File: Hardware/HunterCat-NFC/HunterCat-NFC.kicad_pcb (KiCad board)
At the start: 2 copper layers, 80.7 x 33.5 mm, 71 parts, among them J1 Battery, J2 Conn_01x06_Female, P1 USB_C_Plug_USB2.0, Q1 DMG3415U-7, SW1 RESET, SW2 GPIO, SW3 GPIO1, SW4 GPIO2, SW5 ON, U1 ATSAMD21E18A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

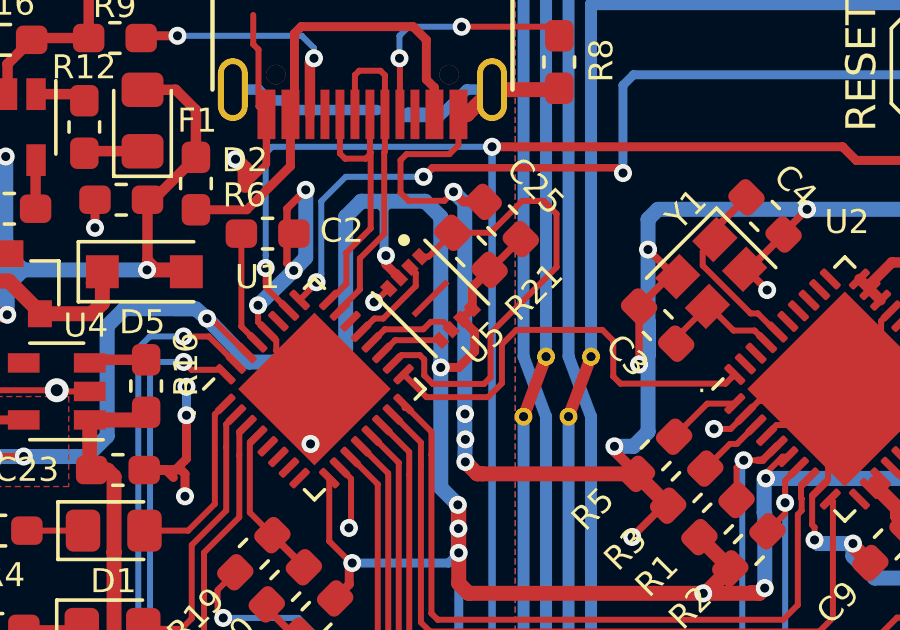
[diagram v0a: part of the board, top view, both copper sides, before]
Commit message: update flash memmory
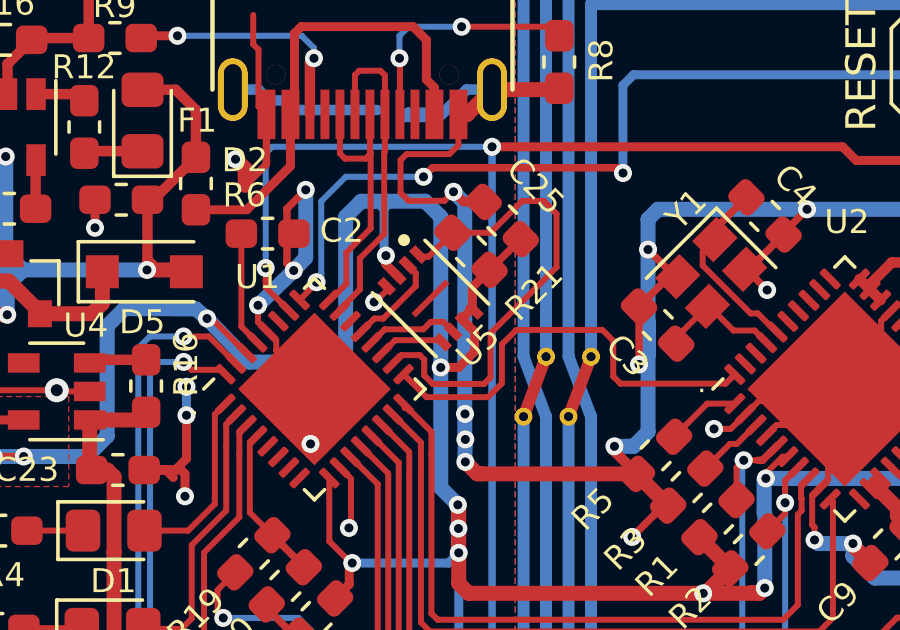
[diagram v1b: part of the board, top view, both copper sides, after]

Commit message: update case
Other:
- rule pad_to_mask_clearance: 0.051 -> 0
- board text added: "V1.3"
- board text removed: "V1.2"
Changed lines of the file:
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@@
   (title_block
     (title "Hunter Cat NFC")
-    (date 2020-11-30)
-    (rev v1.2)
+    (date 2021-01-20)
+    (rev v1.3)
     (company "Electronic Cats")
     (comment 1 "Eduardo Contreras")
@@
     (pad_size 0.65 0.65)
     (pad_drill 0.65)
-    (pad_to_mask_clearance 0.051)
-    (solder_mask_min_width 0.25)
+    (pad_to_mask_clearance 0)
     (aux_axis_origin 0 0)
     (visible_elements 7FFFFFFF)
@@
       (drillshape 0)
       (scaleselection 1)
-      (outputdirectory "gerbers_hunterNFC_v1.2/"))
+      (outputdirectory "gerbers_hunterNFC_v1.3/"))
   )
   (net 0 "")
@@
       (effects (font (size 0.5 0.5) (thickness 0.08)))
     )
-    (pad 2 smd roundrect (at 1.025 0) (size 1.15 1.4) (layers F.Cu F.Paste F.Mask) (roundrect_rratio 0.217391)
+    (pad 2 smd roundrect (at 1.025 0) (size 1.15 1.4) (layers F.Cu F.Paste F.Mask) (roundrect_rratio 0.2173904347826087)
       (net 17 /LED1))
-    (pad 1 smd roundrect (at -1.025 0) (size 1.15 1.4) (layers F.Cu F.Paste F.Mask) (roundrect_rratio 0.217391)
+    (pad 1 smd roundrect (at -1.025 0) (size 1.15 1.4) (layers F.Cu F.Paste F.Mask) (roundrect_rratio 0.2173904347826087)
       (net 18 "Net-(D1-Pad1)"))
     (model ${KISYS3DMOD}/LED_SMD.3dshapes/LED_0805_2012Metric.wrl
@@
       (effects (font (size 0.5 0.5) (thickness 0.08)))
     )
-    (pad 2 smd roundrect (at 1.025 0 90) (size 1.15 1.4) (layers F.Cu F.Paste F.Mask) (roundrect_rratio 0.217391)
+    (pad 2 smd roundrect (at 1.025 0 90) (size 1.15 1.4) (layers F.Cu F.Paste F.Mask) (roundrect_rratio 0.2173904347826087)
       (net 16 VBUS))
-    (pad 1 smd roundrect (at -1.025 0 90) (size 1.15 1.4) (layers F.Cu F.Paste F.Mask) (roundrect_rratio 0.217391)
+    (pad 1 smd roundrect (at -1.025 0 90) (size 1.15 1.4) (layers F.Cu F.Paste F.Mask) (roundrect_rratio 0.2173904347826087)
       (net 19 "Net-(D2-Pad1)"))
     (model ${KISYS3DMOD}/LED_SMD.3dshapes/LED_0805_2012Metric.wrl
@@
       (effects (font (size 0.5 0.5) (thickness 0.08)))
     )
-    (pad 1 smd roundrect (at -1.025 0) (size 1.15 1.4) (layers F.Cu F.Paste F.Mask) (roundrect_rratio 0.217391)
+    (pad 1 smd roundrect (at -1.025 0) (size 1.15 1.4) (layers F.Cu F.Paste F.Mask) (roundrect_rratio 0.2173904347826087)
       (net 21 "Net-(D3-Pad1)"))
-    (pad 2 smd roundrect (at 1.025 0) (size 1.15 1.4) (layers F.Cu F.Paste F.Mask) (roundrect_rratio 0.217391)
+    (pad 2 smd roundrect (at 1.025 0) (size 1.15 1.4) (layers F.Cu F.Paste F.Mask) (roundrect_rratio 0.2173904347826087)
       (net 20 /LED2))
     (model ${KISYS3DMOD}/LED_SMD.3dshapes/LED_0805_2012Metric.wrl
@@
       (effects (font (size 0.5 0.5) (thickness 0.08)))
     )
-    (pad 1 smd roundrect (at -1.025 0) (size 1.15 1.4) (layers F.Cu F.Paste F.Mask) (roundrect_rratio 0.217391)
+    (pad 1 smd roundrect (at -1.025 0) (size 1.15 1.4) (layers F.Cu F.Paste F.Mask) (roundrect_rratio 0.2173904347826087)
       (net 23 "Net-(D4-Pad1)"))
-    (pad 2 smd roundrect (at 1.025 0) (size 1.15 1.4) (layers F.Cu F.Paste F.Mask) (roundrect_rratio 0.217391)
+    (pad 2 smd roundrect (at 1.025 0) (size 1.15 1.4) (layers F.Cu F.Paste F.Mask) (roundrect_rratio 0.2173904347826087)
       (net 22 /LED3))
     (model ${KISYS3DMOD}/LED_SMD.3dshapes/LED_0805_2012Metric.wrl
@@
   (gr_line (start 157.69 108.99) (end 83 109) (layer Edge.Cuts) (width 0.05))
   (gr_line (start 160.69 78.5) (end 160.69 105.99) (layer Edge.Cuts) (width 0.05))
-  (gr_text V1.2 (at 104.91 92.61 90) (layer B.SilkS)
+  (gr_text V1.3 (at 104.91 92.61 90) (layer B.SilkS)
     (effects (font (size 1 1) (thickness 0.2)) (justify mirror))
   )

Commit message: Change_Crystal
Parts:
- Y1: footprint Crystal:Crystal_SMD_2520-4Pin_2.5x2.0mm -> Crystal:Crystal_SMD_2016-4Pin_2.0x1.6mm
- moved C3 0.60 mm to (128.1, 89.7)
- moved Y1 0.46 mm to (129.8, 88.2), turned to 45 degrees
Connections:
- J2 pad 6: Net-(J2-Pad6) -> unconnected-(J2-Pad6)
- U1 pad 22: Net-(U1-Pad22) -> unconnected-(U1-Pad22)
- U1 pad 27: Net-(U1-Pad27) -> unconnected-(U1-Pad27)
- U1 pad 5: Net-(U1-Pad5) -> unconnected-(U1-Pad5)
- U1 pad 6: Net-(U1-Pad6) -> unconnected-(U1-Pad6)
- U1 pad 7: Net-(U1-Pad7) -> unconnected-(U1-Pad7)
- U1 pad 8: Net-(U1-Pad8) -> unconnected-(U1-Pad8)
- U4 pad 4: Net-(U4-Pad4) -> unconnected-(U4-Pad4)
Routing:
- net Net-(C4-Pad1): track 6.28 -> 12.0 mm
- net Net-(C3-Pad1): track 4.15 -> 9.19 mm
- net GND: track 284.8 -> 282.8 mm, vias 43 -> 42
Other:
- net class Default removed

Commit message: update labels for v1.4
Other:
- board text added: "V1.4"
- board text removed: "&"
- board text removed: "Salvador Mendoza"
- board text removed: "V1.3"
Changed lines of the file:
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@@
     (43 "Eco2.User" user "User.Eco2")
     (44 "Edge.Cuts" user)
-    (45 "Margin" user)
+    (45 "Margin" user "Margen")
     (46 "B.CrtYd" user "B.Courtyard")
     (47 "F.CrtYd" user "F.Courtyard")
@@
     (effects (font (size 1.2 1.2) (thickness 0.3)) (justify mirror))
   )
-  (gr_text "Salvador Mendoza" (at 99.61 92.61 90) (layer "B.SilkS")
-    (effects (font (size 1 1) (thickness 0.25)) (justify mirror))
-  )
-  (gr_text "V1.3" (at 104.91 92.61 90) (layer "B.SilkS")
+  (gr_text "V1.4" (at 104.91 92.61 90) (layer "B.SilkS")
     (effects (font (size 1 1) (thickness 0.2)) (justify mirror))
   )
@@
     (effects (font (size 2 2) (thickness 0.5)) (justify mirror))
   )
-  (gr_text "&" (at 96.69 92.37 90) (layer "B.SilkS")
-    (effects (font (size 1 1) (thickness 0.25)) (justify mirror))
-  )
   (gr_text "." (at 129.1 92.03) (layer "F.SilkS")

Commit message: Starting the change of PCB design
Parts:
- added C15: 27pF, Capacitor_SMD:C_0603_1608Metric, F.Cu at (145.4, 72.4)
- added C17: 0.1uF, Capacitor_SMD:C_0603_1608Metric, F.Cu at (155.7, 68.1)
- added C21: 0.1uF, Capacitor_SMD:C_0603_1608Metric, F.Cu at (153.8, 58.1)
- added C22: 1uF, Capacitor_SMD:C_0603_1608Metric, F.Cu at (155.7, 65.6)
- added C25: 0.1uF, Capacitor_SMD:C_0603_1608Metric, F.Cu at (145.4, 69.9)
- added C26: 0.1uF, Capacitor_SMD:C_0603_1608Metric, F.Cu at (143.7, 67.3)
- added C27: 0.1uF, Capacitor_SMD:C_0603_1608Metric, F.Cu at (157.8, 63.1)
- added C28: 0.1uF, Capacitor_SMD:C_0603_1608Metric, F.Cu at (149.4, 69.9)
- added C29: 0.1uF, Capacitor_SMD:C_0603_1608Metric, F.Cu at (157.8, 58.1)
- added C30: 0.1uF, Capacitor_SMD:C_0603_1608Metric, F.Cu at (141.4, 71.9)
- added C31: 0.1uF, Capacitor_SMD:C_0603_1608Metric, F.Cu at (141.4, 74.5)
- added C32: 0.1uF, Capacitor_SMD:C_0603_1608Metric, F.Cu at (161.8, 58.1)
- added R22: 27, Resistor_SMD:R_0603_1608Metric, F.Cu at (151.7, 67.3)
- added R23: 1K, Resistor_SMD:R_0603_1608Metric, F.Cu at (147.7, 67.3)
- added R24: 10K, Resistor_SMD:R_0603_1608Metric, F.Cu at (149.4, 72.4)
- added R7: 1K, Resistor_SMD:R_0603_1608Metric, F.Cu at (161.8, 60.6)
- added SW6: BOOT, Button_Switch_SMD:SW_SPST_TL3342, F.Cu at (136.9, 67.2)
- added Y2: 12Mhz, Crystal:Crystal_SMD_5032-2Pin_5.0x3.2mm, F.Cu at (135.8, 73.1)
- C1: value 0.1uF -> 27pF; footprint Capacitor_SMD:C_0603_1608Metric_Pad1.05x0.95mm_HandSolder -> Capacitor_SMD:C_0603_1608Metric
- C2: footprint Capacitor_SMD:C_0603_1608Metric_Pad1.05x0.95mm_HandSolder -> Capacitor_SMD:C_0603_1608Metric
- R17, R18, R4: value 1K -> 330
- R21: value 10K -> 27; footprint Resistor_SMD:R_0603_1608Metric_Pad1.05x0.95mm_HandSolder -> Resistor_SMD:R_0603_1608Metric
- U1: value ATSAMD21E18A -> RP2040; footprint Package_DFN_QFN:QFN-32-1EP_5x5mm_P0.5mm_EP3.6x3.6mm -> RP2040:RP2040-QFN-56
- U5: value GD25Q16CEIGR -> W25Q16JV; footprint hunter-cat-nfc:PSON50P200X300X50-9N -> Package_SO:SOIC-8_5.275x5.275mm_P1.27mm
- moved C1 52.5 mm to (153.8, 63.1), turned to 0 degrees
- moved C2 47.3 mm to (153.8, 60.6)
- moved R21 45.4 mm to (157.8, 60.6), turned to 0 degrees
- moved U5 33.8 mm to (137.3, 60.2), turned to 0 degrees
- moved R19 5.96 mm to (113.4, 103.7), turned to 0 degrees
- moved Re 3.82 mm to (113.4, 102.2), turned to 180 degrees
- moved U1 3.46 mm to (116.5, 95.7), turned to 0 degrees
- moved D4 2.62 mm to (109.5, 100.8)
- moved R18 2.62 mm to (105.6, 100.7)
- moved J2 2.42 mm to (118.5, 106.1)
- moved D3 1.40 mm to (109.5, 98.8)
- moved R17 1.40 mm to (105.6, 98.8)
- moved C25 0.42 mm to (122.8, 86.4)
- renumbered R20 to Re
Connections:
- C1 pad 1: +3V3 -> Net-(C1-Pad1)
- C2 pad 1: Net-(C2-Pad1) -> +1V2
- R21 pad 1: +3V3 -> /D+
- R21 pad 2: /CS -> /RD+
- U1 pad 1: /LED1 -> +3V3
- U1 pad 10: GND -> +3V3
- U1 pad 11: /SDA -> unconnected-(U1-Pad11)
- U1 pad 12: /SCL -> unconnected-(U1-Pad12)
- U1 pad 13: /GPIO2 -> unconnected-(U1-Pad13)
- U1 pad 14: /GPIO1 -> unconnected-(U1-Pad14)
- U1 pad 15: /VEN -> unconnected-(U1-Pad15)
- U1 pad 16: /IRQ -> unconnected-(U1-Pad16)
- U1 pad 17: /CLK -> /VEN
- U1 pad 18: /CS -> /IRQ
- U1 pad 19: /MOSI -> GND
- U1 pad 2: /LED2 -> /TX
- U1 pad 20: /SCK -> Net-(C1-Pad1)
- U1 pad 21: /MISO -> Net-(R7-Pad2)
- U1 pad 22: unconnected-(U1-Pad22) -> +3V3
- U1 pad 23: /D- -> +1V2
- U1 pad 24: /D+ -> /SWCLK
- U1 pad 25: /GPIO -> /SWDIO
- U1 pad 27: unconnected-(U1-Pad27) -> /CLK
- U1 pad 28: GND -> /GPIO
- U1 pad 29: Net-(C2-Pad1) -> unconnected-(U1-Pad29)
- U1 pad 3: /LED3 -> /RX
- U1 pad 30: +3V3 -> unconnected-(U1-Pad30)
- U1 pad 31: /SWCLK -> unconnected-(U1-Pad31)
- U1 pad 32: /SWDIO -> /GPIO1
- U1 pad 4: /B_ADC -> unconnected-(U1-Pad4)
- U1 pad 6: unconnected-(U1-Pad6) -> /SDA
- U1 pad 7: unconnected-(U1-Pad7) -> /SCL
- U1 pad 9: +3V3 -> unconnected-(U1-Pad9)
- U4 pad 3: Net-(R16-Pad2) -> Net-(C23-Pad1)
- U5 pad 1: /CS -> /QSPI_CS
- U5 pad 2: /MISO -> /QSPI_DATA1
- U5 pad 3: +3V3 -> /QSPI_DATA2
- U5 pad 5: /MOSI -> /QSPI_DATA0
- U5 pad 6: /SCK -> /QSPI_SCK
- U5 pad 7: +3V3 -> /QSPI_DATA3
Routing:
- net GND: track 282.8 -> 257.1 mm, vias 42 -> 32
- net +3V3: track 134.0 -> 109.3 mm, vias 17 -> 16
- net /SWCLK: track 25.4 -> 1.84 mm, vias 2 -> 0
- net /VEN: track 25.4 -> 2.20 mm
- net /IRQ: track 24.2 -> 1.84 mm
- net /CS: track 16.6 -> 0.00 mm
- net /RST: track 62.5 -> 49.0 mm, vias 3 -> 2
- net /SWDIO: track 19.8 -> 6.59 mm, vias 2 -> 0
- net +BATT: track 56.1 -> 44.9 mm
- net /LED3: track 12.2 -> 1.44 mm
- net /CLK: track 14.6 -> 3.94 mm
- net /LED2: track 9.17 -> 1.76 mm
- net /SCL: track 29.9 -> 22.7 mm
- net /SDA: track 30.2 -> 23.0 mm
- net /GPIO2: track 43.5 -> 36.3 mm
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
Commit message: update layout to 3.0v
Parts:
- removed the C25 at (122.8, 86.4)
- removed J2: Conn_01x06_Female, Connector:Tag-Connect_TC2030-IDC-NL_2x03_P1.27mm_Vertical
- removed R16: 10K, Resistor_SMD:R_0603_1608Metric_Pad1.05x0.95mm_HandSolder
- removed R23: 1K, Resistor_SMD:R_0603_1608Metric
- removed Re: 100K, Resistor_SMD:R_0603_1608Metric_Pad1.05x0.95mm_HandSolder
- removed SW6: BOOT, Button_Switch_SMD:SW_SPST_TL3342
- added JP1: BOOT, Jumper:SolderJumper-2_P1.3mm_Open_TrianglePad1.0x1.5mm, B.Cu at (113.1, 87.5)
- added R20: 100K, Resistor_SMD:R_0603_1608Metric, F.Cu at (109.1, 76.7)
- C10, C11, C12, C13, C14, C16, C18, C19, C20, C23, C24, C3, C4, C5, C6, C7, C8, C9: footprint Capacitor_SMD:C_0603_1608Metric_Pad1.05x0.95mm_HandSolder -> Capacitor_SMD:C_0603_1608Metric
- R1, R10, R11, R12, R13, R14, R15, R17, R18, R19, R2, R3, R4, R5, R6, R8, R9: footprint Resistor_SMD:R_0603_1608Metric_Pad1.05x0.95mm_HandSolder -> Resistor_SMD:R_0603_1608Metric
- U5: footprint Package_SO:SOIC-8_5.275x5.275mm_P1.27mm -> hunter-cat-nfc:W25Q16JVUUIQ
- Y2: footprint Crystal:Crystal_SMD_5032-2Pin_5.0x3.2mm -> Crystal:Crystal_SMD_2520-4Pin_2.5x2.0mm
- moved R7 61.1 mm to (116.1, 101.1)
- moved C1 58.1 mm to (111.9, 103.3), turned to 90 degrees
- moved C27 54.4 mm to (120.5, 102.6)
- moved C22 54.1 mm to (109.7, 94.0), turned to -90 degrees
- moved C32 53.6 mm to (116.0, 86.0), turned to 90 degrees
- moved C2 52.5 mm to (120.5, 101.2)
- moved C29 49.1 mm to (117.5, 86.0), turned to 90 degrees
- moved R21 48.2 mm to (118.9, 88.9), turned to -90 degrees
- moved C21 44.4 mm to (121.8, 88.9), turned to 90 degrees
- moved C28 44.4 mm to (111.5, 93.0), turned to 90 degrees
- moved C17 44.2 mm to (116.8, 89.0), turned to 90 degrees
- moved C26 43.5 mm to (120.5, 104.1)
- moved C15 42.2 mm to (116.8, 103.3), turned to -90 degrees
- moved C30 39.6 mm to (120.5, 105.6)
- moved R24 38.3 mm to (113.4, 85.5), turned to 180 degrees
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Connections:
- U1 pad 11: unconnected-(U1-Pad11) -> /LED1
- U1 pad 12: unconnected-(U1-Pad12) -> /LED2
- U1 pad 13: unconnected-(U1-Pad13) -> /LED3
- U1 pad 17: /VEN -> unconnected-(U1-Pad17)
- U1 pad 18: /IRQ -> unconnected-(U1-Pad18)
- U1 pad 27: /CLK -> unconnected-(U1-Pad27)
- U1 pad 28: /GPIO -> /VEN
- U1 pad 29: unconnected-(U1-Pad29) -> /IRQ
- U1 pad 30: unconnected-(U1-Pad30) -> /GPIO2
- U1 pad 31: unconnected-(U1-Pad31) -> /GPIO
- U1 pad 34: /GPIO2 -> unconnected-(U1-Pad34)
- U1 pad 37: /LED1 -> unconnected-(U1-Pad37)
- U1 pad 39: /LED2 -> unconnected-(U1-Pad39)
- U1 pad 40: /LED3 -> unconnected-(U1-Pad40)
- U2 pad 40: /CLK -> unconnected-(U2-Pad40)
- Y2 pad 2: Net-(C15-Pad1) -> GND
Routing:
- net +3V3: track 109.3 -> 153.2 mm, vias 16 -> 11
- net /B_ADC: track 1.50 -> 42.0 mm, vias 0 -> 2
- net +BATT: track 44.9 -> 11.5 mm, vias 2 -> 0
- net +1V2: track 0.00 -> 25.3 mm
- net /VEN: track 2.20 -> 19.1 mm
- net /IRQ: track 1.84 -> 18.1 mm
- net /QSPI_CS: track 0.00 -> 13.5 mm, vias 0 -> 1
- net /SCL: track 22.7 -> 35.4 mm, vias 2 -> 4
- net /SDA: track 23.0 -> 35.1 mm, vias 2 -> 4
- net /GPIO: track 43.4 -> 52.8 mm, vias 4 -> 5
- net /QSPI_DATA1: track 0.00 -> 8.32 mm
- net /RST: track 49.0 -> 40.7 mm
- net Net-(C1-Pad1): track 0.00 -> 7.72 mm
- net /QSPI_DATA2: track 0.00 -> 7.49 mm
- net Net-(C23-Pad1): track 16.9 -> 24.0 mm
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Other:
- board text added: "2.0v"
- board text removed: "V1.4"

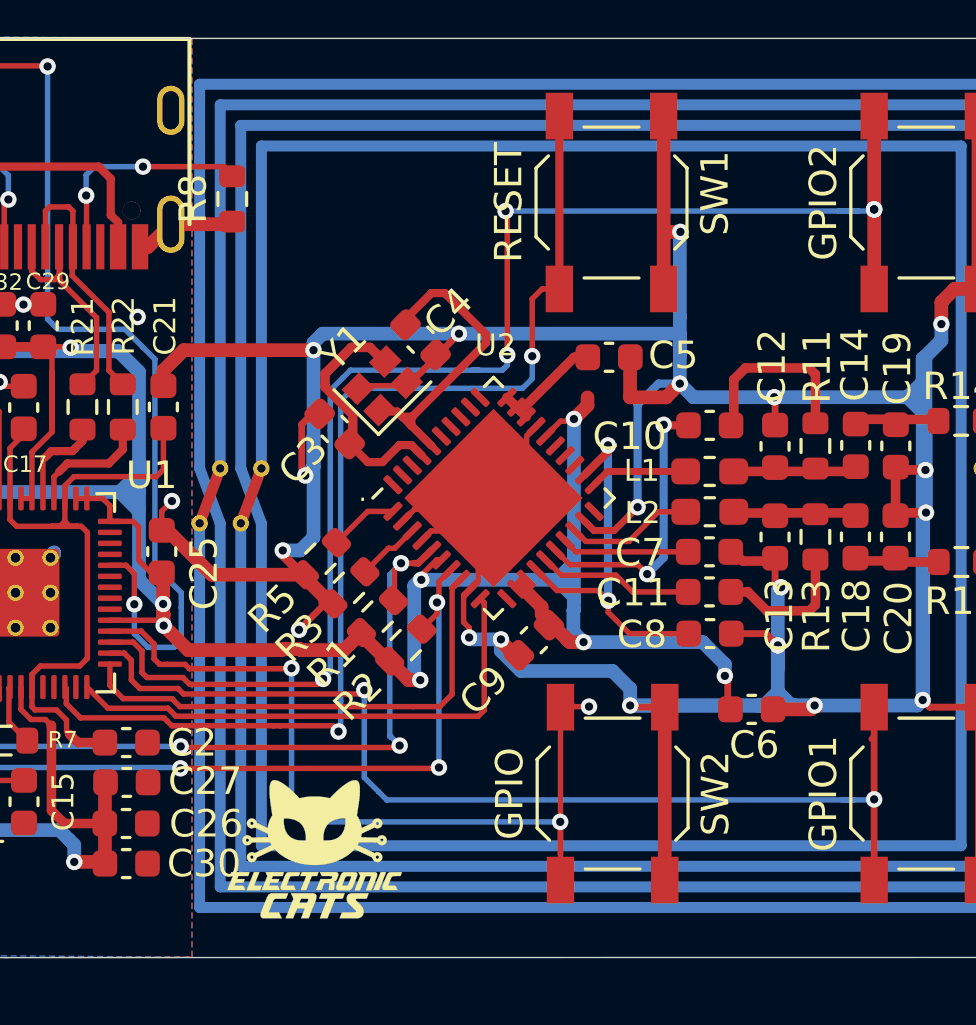
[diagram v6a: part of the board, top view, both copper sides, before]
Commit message: update labels v2.040
version for RP2040
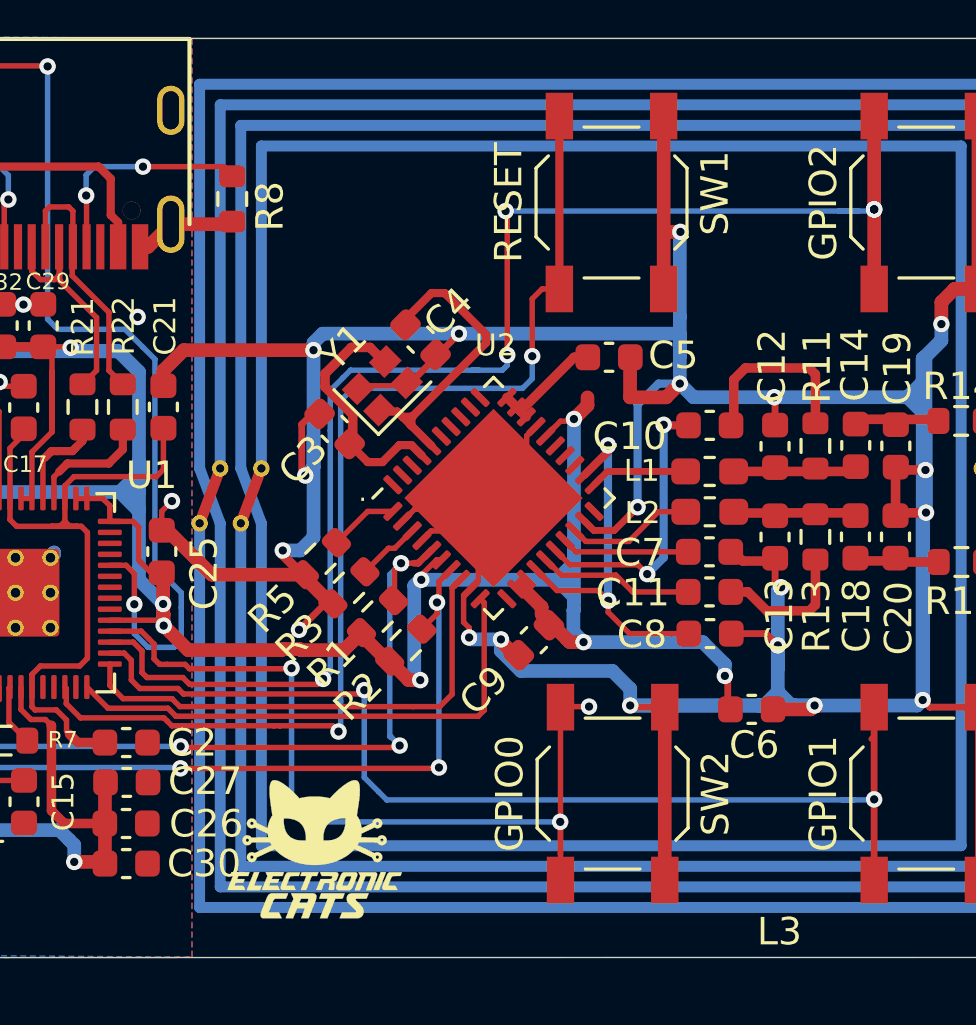
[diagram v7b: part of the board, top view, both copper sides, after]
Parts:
- added kibuzzard-62BD092C: G***, kibuzzard-62BD092C, B.Cu at (113.0, 90.4)
- SW2: value GPIO -> GPIO0
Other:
- board text added: "V2.040"
- board text removed: "2.0v"
